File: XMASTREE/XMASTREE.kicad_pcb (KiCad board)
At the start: 2 copper layers, 42.2 x 70.3 mm, 0 parts

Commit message: set up board
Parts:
- added BT1: ~, XMAS:C2032, B.Cu at (42.4, 69.0)
- added C1: 10u, Capacitor_SMD:C_0805_2012Metric_Pad1.15x1.40mm_HandSolder, F.Cu at (73.7, 41.3)
- added D1: LED, LED_SMD:LED_0805_2012Metric_Pad1.15x1.40mm_HandSolder, F.Cu at (73.7, 35.2)
- added D2: LED, LED_SMD:LED_0805_2012Metric_Pad1.15x1.40mm_HandSolder, F.Cu at (84.4, 27.5)
- added D3: LED, LED_SMD:LED_0805_2012Metric_Pad1.15x1.40mm_HandSolder, F.Cu at (91.3, 21.3)
- added D4: LED, LED_SMD:LED_0805_2012Metric_Pad1.15x1.40mm_HandSolder, F.Cu at (73.7, 38.3)
- added D5: LED, LED_SMD:LED_0805_2012Metric_Pad1.15x1.40mm_HandSolder, F.Cu at (78.5, 35.2)
- added D6: LED, LED_SMD:LED_0805_2012Metric_Pad1.15x1.40mm_HandSolder, F.Cu at (84.4, 30.5)
- added Q1: Q_NMOS_GSD, Package_TO_SOT_SMD:SOT-23_Handsoldering, F.Cu at (85.7, 22.1)
- added R1: 1K, Resistor_SMD:R_0805_2012Metric_Pad1.15x1.40mm_HandSolder, F.Cu at (89.2, 25.8)
- added R2: 1K, Resistor_SMD:R_0805_2012Metric_Pad1.15x1.40mm_HandSolder, F.Cu at (78.5, 38.2)
- added R3: 1K, Resistor_SMD:R_0805_2012Metric_Pad1.15x1.40mm_HandSolder, F.Cu at (83.2, 35.2)
- added R4: 1K, Resistor_SMD:R_0805_2012Metric_Pad1.15x1.40mm_HandSolder, F.Cu at (73.7, 44.2)
- added R5: 1K, Resistor_SMD:R_0805_2012Metric_Pad1.15x1.40mm_HandSolder, F.Cu at (89.2, 28.8)
- added R6: 1K, Resistor_SMD:R_0805_2012Metric_Pad1.15x1.40mm_HandSolder, F.Cu at (78.5, 41.2)
- added R7: 100k, Resistor_SMD:R_0805_2012Metric_Pad1.15x1.40mm_HandSolder, F.Cu at (93.9, 24.3)
- added R8: 100K, Resistor_SMD:R_0805_2012Metric_Pad1.15x1.40mm_HandSolder, F.Cu at (93.9, 27.3)
- added R9: 100K, Resistor_SMD:R_0805_2012Metric_Pad1.15x1.40mm_HandSolder, F.Cu at (96.1, 21.3)
- added SW1: SW_SPDT, XMAS:2.54mm_4x9mm_SPDT, F.Cu at (116.2, 40.0)
- added TP1: Front side decoratoins, XMAS:Decorations, F.Cu at (42.4, 21.6)
- added TP2: Back side decorations, XMAS:Decorations, B.Cu at (42.4, 21.6)
- added U1: TLC555, Package_SO:SO-8_5.3x6.2mm_P1.27mm, F.Cu at (76.6, 29.8)
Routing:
- added copper zone on F.Cu, net +BATT
- added copper zone on B.Cu, net GND

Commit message: -
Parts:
- C1, R7, R8, R9, SW1, U1: moved to B.Cu
- moved SW1 84.8 mm to (42.5, 82.0), turned to 180 degrees
- moved R1 74.4 mm to (33.7, 75.4), turned to 180 degrees
- moved R9 65.7 mm to (35.5, 46.8), turned to 180 degrees
- moved D1 63.5 mm to (25.9, 77.0)
- moved D2 55.2 mm to (31.0, 41.5), turned to 180 degrees
- moved Q1 53.0 mm to (39.2, 47.7), turned to 90 degrees
- moved D6 53.0 mm to (58.9, 77.0)
- moved R7 50.0 mm to (49.3, 46.8), turned to 180 degrees
- moved D4 49.9 mm to (27.4, 57.0)
- moved D3 49.2 mm to (57.4, 57.0)
- moved R8 47.9 mm to (49.3, 44.8)
- moved R5 46.1 mm to (45.9, 44.6)
- moved R6 44.0 mm to (51.3, 75.8)
- moved R3 43.6 mm to (46.6, 58.8)
- moved R4 39.6 mm to (38.9, 63.1)
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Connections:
- net Net-(BT1-Pad1) renamed /BTN_COM
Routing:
- net /BTN_COM: track 0.00 -> 22.3 mm
- net Net-(D2-Pad2): track 0.00 -> 15.8 mm
- net Net-(D1-Pad1): track 0.00 -> 14.0 mm, vias 0 -> 1
- net Net-(C1-Pad1): track 0.00 -> 12.4 mm
- net +BATT: track 0.00 -> 10.00 mm, vias 0 -> 2
- net Net-(R7-Pad2): track 0.00 -> 4.51 mm
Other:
- outline, holes or cut-outs redrawn
- net class power added: clearance 0.2, trace_width 0.5, via_dia 0.8, via_drill 0.4

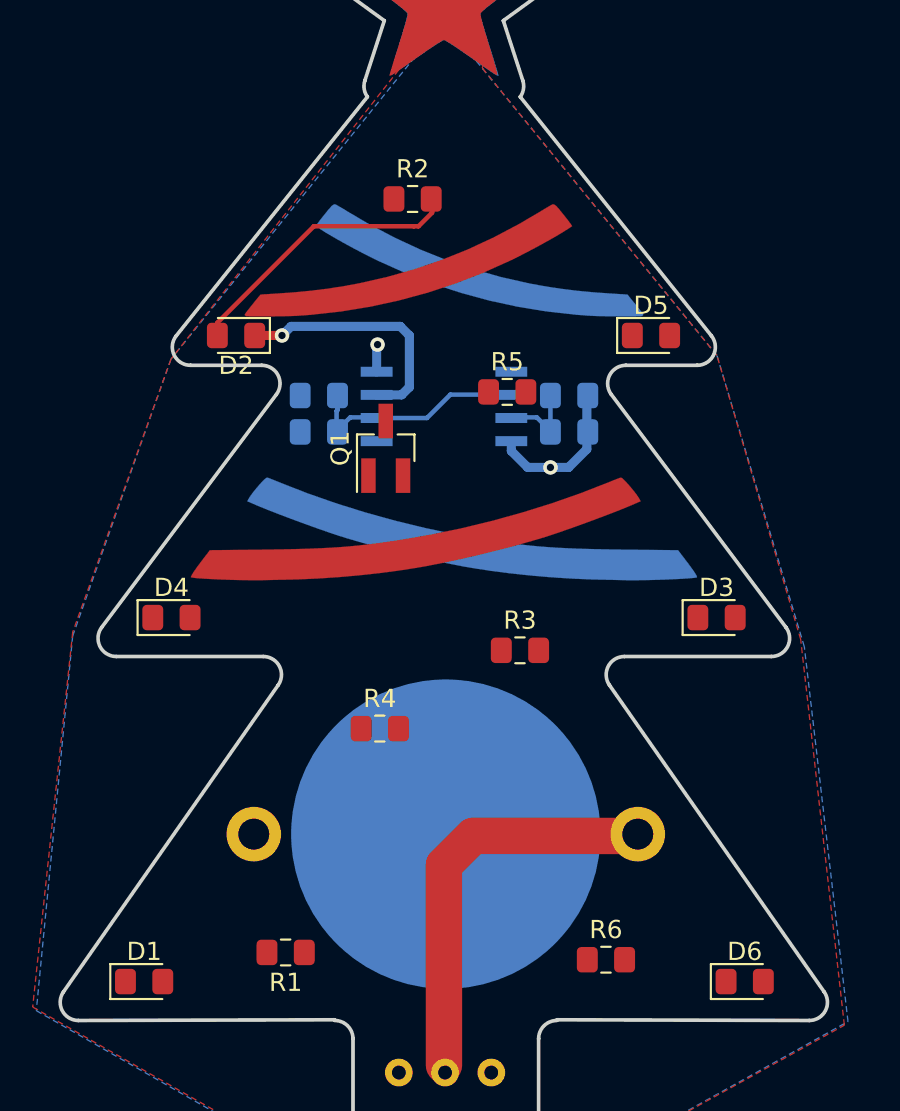
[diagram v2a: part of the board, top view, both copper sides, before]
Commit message: angled leds
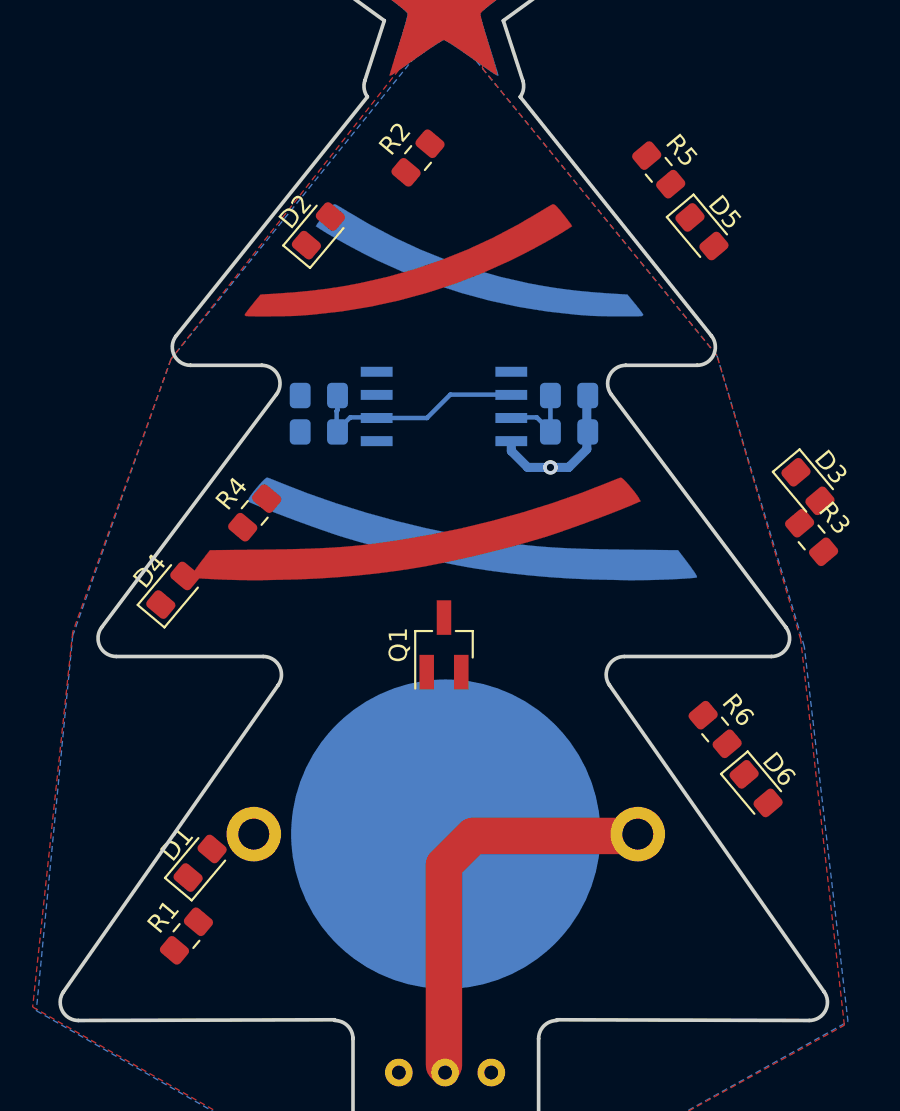
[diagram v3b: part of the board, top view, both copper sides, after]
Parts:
- moved R3 17.2 mm to (62.6, 52.6), turned to 310 degrees
- moved R5 14.8 mm to (54.2, 32.4), turned to 310 degrees
- moved R6 14.0 mm to (57.3, 63.1), turned to 310 degrees
- moved R4 13.7 mm to (32.0, 51.2), turned to 50 degrees
- moved Q1 11.3 mm to (42.4, 58.5)
- moved D6 10.6 mm to (59.5, 66.4), turned to 310 degrees
- moved D3 8.78 mm to (62.4, 49.8), turned to 310 degrees
- moved D2 7.32 mm to (35.5, 35.8), turned to 50 degrees
- moved D1 7.19 mm to (29.0, 70.5), turned to 50 degrees
- moved D5 6.35 mm to (56.6, 35.8), turned to 310 degrees
- moved R1 5.52 mm to (28.2, 74.5), turned to 50 degrees
- moved R2 2.27 mm to (41.0, 31.8), turned to 50 degrees
- moved D4 1.50 mm to (27.5, 55.5), turned to 50 degrees
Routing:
- net Net-(D2-Pad2): track 15.8 -> 0.00 mm
- net Net-(D1-Pad1): track 14.0 -> 0.00 mm, vias 1 -> 0
- net +BATT: track 10.00 -> 8.48 mm, vias 2 -> 1

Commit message: layout mostly complete
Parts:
- moved R6 12.5 mm to (55.8, 75.6)
- moved e 10.9 mm to (51.8, 54.2)
- moved D6 9.45 mm to (58.7, 75.8)
- moved R5 9.25 mm to (48.9, 40.0)
- moved D3 8.88 mm to (54.8, 54.4), turned to 130 degrees
- moved D4 7.50 mm to (33.0, 50.4)
- moved D5 6.40 mm to (51.9, 40.2), turned to 130 degrees
- moved D1 6.07 mm to (26.1, 75.8)
- moved R4 4.24 mm to (36.1, 50.0)
- moved R2 3.52 mm to (39.7, 35.0)
- moved C1 2.90 mm to (34.3, 47.4), turned to 270 degrees
- moved R8 1.67 mm to (48.4, 43.4), turned to 90 degrees
- moved R1 1.38 mm to (29.1, 75.6)
- moved D2 1.15 mm to (36.6, 35.4)
- moved R7 1.08 mm to (48.4, 47.4), turned to 90 degrees
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- renumbered R3 to e
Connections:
- net Net-(D1-Pad1) renamed /OUTPUT
- net Net-(D4-Pad1) renamed /INVERTED
- TP1 pad 1: +BATT -> Net-(TP1-Pad1)
- TP2 pad 1: GND -> Net-(TP2-Pad1)
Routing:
- net /OUTPUT: track 0.00 -> 100.2 mm, vias 0 -> 1
- net /INVERTED: track 0.00 -> 77.6 mm, vias 0 -> 2
- net GND: track 0.00 -> 12.7 mm, vias 0 -> 4
- net Net-(R7-Pad2): track 4.51 -> 15.2 mm
- net +BATT: track 8.48 -> 13.4 mm, vias 1 -> 2
- net Net-(D4-Pad2): track 0.00 -> 3.08 mm
- net Net-(D2-Pad2): track 0.00 -> 3.08 mm
- net Net-(D1-Pad2): track 0.00 -> 3.01 mm
- net Net-(D6-Pad2): track 0.00 -> 2.95 mm
- net Net-(D3-Pad2): track 0.00 -> 2.17 mm
- net Net-(D5-Pad2): track 0.00 -> 2.17 mm
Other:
- board size 42.2 x 70.3 mm -> 42.2 x 70.2 mm

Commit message: REV A
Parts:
- renumbered R7 to 100K, R8 to 100K, R9 to 100K, U1 to 555
